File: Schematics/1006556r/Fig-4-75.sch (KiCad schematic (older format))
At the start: 0 parts

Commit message: For module A31, transcribed through Fig 4-87, leaving just 88, 91, 93, 114, 141, and 147 to go, plus their integration into the top-level sheet (and resolution of remaining inconsistencies in ND-1021041).
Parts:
- added J1: ConnectorGeneric, symbol AGC_DSKY:ConnectorGeneric
- added U? (x14): D3NOR-+3VDC-0VDC-nd1021041-A_C-___, symbol D3NOR-+3VDC-0VDC-nd1021041:D3NOR-+3VDC-0VDC-nd1021041-A_C-___
- added U? (x4): D3NOR-+3VDC-0VDC-nd1021041-ABC-___, symbol D3NOR-+3VDC-0VDC-nd1021041:D3NOR-+3VDC-0VDC-nd1021041-ABC-___
- added U? (x4): D3NOR-NC-0VDC-expander-nd1021041-A_C-___, symbol D3NOR-NC-0VDC-expander-nd1021041:D3NOR-NC-0VDC-expander-nd1021041-A_C-___
- added U?: D3NOR-+3VDC-0VDC-nd1021041-_B_-___, symbol D3NOR-+3VDC-0VDC-nd1021041:D3NOR-+3VDC-0VDC-nd1021041-_B_-___
- added U?: D3NOR-NC-0VDC-expander-nd1021041-ABC-___, symbol D3NOR-NC-0VDC-expander-nd1021041:D3NOR-NC-0VDC-expander-nd1021041-ABC-___
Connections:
- net +3VDC: now also U?.6 (+3VDC), U?.6 (+3VDC), U?.6 (+3VDC), U?.6 (+3VDC), U?.6 (+3VDC), U?.6 (+3VDC), U?.6 (+3VDC), U?.6 (+3VDC), U?.6 (+3VDC), U?.6 (+3VDC), U?.6 (+3VDC), U?.6 (+3VDC), U?.6 (+3VDC), U?.6 (+3VDC), U?.6 (+3VDC), U?.6 (+3VDC), U?.6 (+3VDC), U?.6 (+3VDC), U?.6 (+3VDC)
- net 0VDC: now also U?.2 (0VDC), U?.3 (0VDC), U?.3 (0VDC), U?.3 (0VDC), U?.3 (0VDC), U?.3 (0VDC), U?.3 (0VDC), U?.3 (0VDC), U?.3 (0VDC), U?.3 (0VDC), U?.3 (0VDC), U?.3 (0VDC), U?.3 (0VDC), U?.3 (0VDC), U?.3 (0VDC), U?.3 (0VDC), U?.3 (0VDC), U?.3 (0VDC), U?.3 (0VDC), U?.4 (0VDC), U?.5 (0VDC), U?.5 (0VDC), U?.5 (0VDC), U?.5 (0VDC), U?.5 (0VDC), U?.5 (0VDC), U?.5 (0VDC), U?.5 (0VDC), U?.5 (0VDC), U?.5 (0VDC), U?.5 (0VDC), U?.5 (0VDC), U?.5 (0VDC), U?.5 (0VDC), U?.5 (0VDC), U?.5 (0VDC), U?.5 (0VDC), U?.5 (0VDC), U?.5 (0VDC), U?.5 (0VDC), U?.5 (0VDC), U?.5 (0VDC), U?.5 (0VDC), U?.5 (0VDC)
- new net: J1.81, U?.1 (J), U?.2 (C)
- new net: J1.63, U?.2 (C)
- new net: J1.82, U?.4 (A)
- new net: J1.85, U?.2 (C)
- new net: J1.116, U?.4 (A)
- new net: J1.139, U?.4 (A), U?.4 (A)
- new net: J1.89, U?.4 (A)
- new net: J1.137, U?.4 (A)
- new net: J1.61, U?.2 (C)
- new net: J1.135, U?.2 (C)
- new net: J1.41, U?.4 (A), U?.4 (A)
- new net: J1.65, U?.4 (A)
- new net: J1.42, U?.1 (J)
- new net: U?.1 (J), U?.4 (A) (x4)
- new net: U?.1 (J), U?.3 (B) (x2)
- new net: J1.123, U?.2 (C), U?.3 (B)
- new net: J1.53, U?.2 (C), U?.4 (A)
- new net: U?.1 (J), U?.2 (C) (x4)
- new net: J1.136, U?.4 (A), U?.4 (A), U?.4 (A)
- new net: J1.44, U?.2 (C)
- new net: J1.46, U?.4 (A)
- new net: U?.1 (J), U?.2 (C), U?.3 (B)
- new net: J1.83, U?.3 (B)
- new net: U?.1 (J), U?.2 (C), U?.2 (C)
- new net: J1.100, U?.2 (C)
- new net: J1.98, U?.2 (C)
- new net: J1.86, U?.1 (J), U?.1 (J)
- new net: J1.50, U?.2 (C)
- new net: J1.57, U?.1 (J), U?.3 (B)
- new net: J1.69, U?.4 (A)
- new net: J1.109, U?.4 (A)
- new net: J1.103, U?.2 (C)
- new net: J1.101, U?.1 (J)
- new net: J1.104, U?.2 (C)
- new net: J1.105, U?.2 (C)
- new net: J1.67, U?.2 (C)
- new net: J1.73, U?.1 (J), U?.1 (J)
- new net: J1.99, U?.2 (C)
- new net: U?.1 (J), U?.4 (A), U?.4 (A)
- new net: U?.1 (J), U?.1 (J), U?.4 (A)
- new net: J1.77, U?.1 (J)
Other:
- note added: "Notes from the Virtual AGC Project:\n5. Figure 4-75 duplicates the circuits for gates 60007 and\n 60056, but is not internally consistent with respect to\n either the type of gate or the numbering of the connector\n pins feeding the gates. The numbering has been \n reconciled by referencing the other ND-1021041 Figures\n comprising module A21. — RSB 2018"

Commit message: Finished up transcription of drawing 1006556 (Block I logic flow S, module A21).  But it may be a total mess, so user beware!
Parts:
- removed unit 63 of J1
- removed unit 82 of J1
- removed unit 116 of J1
- removed unit 139 of J1
- removed unit 89 of J1
- removed unit 137 of J1
- removed unit 61 of J1
- removed unit 41 of J1
- removed unit 65 of J1
- removed unit 53 of J1
- removed unit 83 of J1
- removed unit 50 of J1
- removed unit 109 of J1
- removed unit 103 of J1
- removed unit 67 of J1
- removed unit 123 of J1
- removed unit 98 of J1
- removed unit 99 of J1
- removed unit 136 of J1
- removed U? (x6): D3NOR-+3VDC-0VDC-nd1021041-A_C-___, symbol D3NOR-+3VDC-0VDC-nd1021041:D3NOR-+3VDC-0VDC-nd1021041-A_C-___
- gave numbers to parts that had none: 18
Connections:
- net T04_B: now reaches U610.4 (A)
- net BR1: now reaches U603.4 (A)
- net T02_: now reaches U609.4 (A)
- net G06: now reaches U602.4 (A)
- net g60052: now reaches J1.42, U605.1 (J)
- net g60031: now reaches U609.1 (J), U612.4 (A)
- net g60014: now reaches U611.3 (B)
- net MP1_: now reaches U616.3 (B)
- net T01_: now reaches U608.2 (C)
- net g60034: now reaches U611.2 (C)
- net T04_: now reaches U605.4 (A), U606.4 (A), U607.4 (A)
- net g60056: now reaches U610.1 (J), U612.2 (C), U615.3 (B)
- net TS0_: now reaches U610.3 (B)
- net g60057: now reaches U606.1 (J), U613.2 (C), U615.2 (C)
- net g60072: now reaches U614.2 (C)
- net T03_: now reaches U616.4 (A)
- net g60062: now reaches U617.2 (C)
- net g60067: now reaches U612.3 (B)
- net STD2: now reaches U601.2 (C)
- net g60048: now reaches U613.4 (A)
- net TC: now reaches U602.2 (C)
- net g60047: now reaches U616.1 (J), U617.4 (A)

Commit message: When I started recovering transcribed Block I schematics from document ND-1021041, there was no info available to me on the pinout of the NOR-gates they used, and it didn't occur to me that any might be forthcoming, so I chose a pinout arbitrarily.  It turns out that we now have the required info (SCD 1006771), and my arbitrary choices were wrong. I've therefore updated the NOR-library generator script, the relevant NOR libraries themselves, and all of the so-far-recovered Block I schematics using those gates.  It doesn't really matter in the cosmic sense, since the real Block I schematics have become available in the meantime, so that these recovered schematics are of less interest, but it will come in handy when I eventually want to do cross-checking.  I haven't checked these updated schematics in full detail, but I've spot-checked them, and run some ERCs and netlists, and it looks good to me.
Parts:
- U601, U613, U614, U617: value D3NOR-NC-0VDC-expander-nd1021041-A_C-___ -> D3NOR-NC-0VDC-expander-nd1021041-1_5-___; symbol D3NOR-NC-0VDC-expander-nd1021041:D3NOR-NC-0VDC-expander-nd1021041-A_C-___ -> D3NOR-NC-0VDC-expander-nd1021041:D3NOR-NC-0VDC-expander-nd1021041-1_5-___
- U602, U603, U604, U605, U606, U607, U608, U609: value D3NOR-+3VDC-0VDC-nd1021041-A_C-___ -> D3NOR-+3VDC-0VDC-nd1021041-1_5-___; symbol D3NOR-+3VDC-0VDC-nd1021041:D3NOR-+3VDC-0VDC-nd1021041-A_C-___ -> D3NOR-+3VDC-0VDC-nd1021041:D3NOR-+3VDC-0VDC-nd1021041-1_5-___
- U610, U611, U615, U616: value D3NOR-+3VDC-0VDC-nd1021041-ABC-___ -> D3NOR-+3VDC-0VDC-nd1021041-135-___; symbol D3NOR-+3VDC-0VDC-nd1021041:D3NOR-+3VDC-0VDC-nd1021041-ABC-___ -> D3NOR-+3VDC-0VDC-nd1021041:D3NOR-+3VDC-0VDC-nd1021041-135-___
- U612: value D3NOR-NC-0VDC-expander-nd1021041-ABC-___ -> D3NOR-NC-0VDC-expander-nd1021041-135-___; symbol D3NOR-NC-0VDC-expander-nd1021041:D3NOR-NC-0VDC-expander-nd1021041-ABC-___ -> D3NOR-NC-0VDC-expander-nd1021041:D3NOR-NC-0VDC-expander-nd1021041-135-___
- U618: value D3NOR-+3VDC-0VDC-nd1021041-_B_-___ -> D3NOR-+3VDC-0VDC-nd1021041-_3_-___; symbol D3NOR-+3VDC-0VDC-nd1021041:D3NOR-+3VDC-0VDC-nd1021041-_B_-___ -> D3NOR-+3VDC-0VDC-nd1021041:D3NOR-+3VDC-0VDC-nd1021041-_3_-___
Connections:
- net +3VDC: now also U602.8 (+3VDC), U603.8 (+3VDC), U604.8 (+3VDC), U605.8 (+3VDC), U606.8 (+3VDC), U607.8 (+3VDC), U608.8 (+3VDC), U609.8 (+3VDC), U610.8 (+3VDC), U611.8 (+3VDC), U615.8 (+3VDC), U616.8 (+3VDC), U618.8 (+3VDC); no longer U602.6 (+3VDC), U603.6 (+3VDC), U604.6 (+3VDC), U605.6 (+3VDC), U606.6 (+3VDC), U607.6 (+3VDC), U608.6 (+3VDC), U609.6 (+3VDC), U610.6 (+3VDC), U611.6 (+3VDC), U615.6 (+3VDC), U616.6 (+3VDC), U618.6 (+3VDC)
- net 0VDC: now also U601.4 (0VDC), U602.4 (0VDC), U603.4 (0VDC), U604.4 (0VDC), U605.4 (0VDC), U606.4 (0VDC), U607.4 (0VDC), U608.4 (0VDC), U609.4 (0VDC), U610.4 (0VDC), U611.4 (0VDC), U612.4 (0VDC), U613.4 (0VDC), U614.4 (0VDC), U615.4 (0VDC), U616.4 (0VDC), U617.4 (0VDC), U618.1 (0VDC); no longer U601.5 (0VDC), U602.5 (0VDC), U603.5 (0VDC), U604.5 (0VDC), U605.5 (0VDC), U606.5 (0VDC), U607.5 (0VDC), U608.5 (0VDC), U609.5 (0VDC), U610.5 (0VDC), U611.5 (0VDC), U612.5 (0VDC), U613.5 (0VDC), U614.5 (0VDC), U615.5 (0VDC), U616.5 (0VDC), U617.5 (0VDC), U618.2 (0VDC)
- net BR1: now also U603.1; no longer U603.4 (A)
- net G06: now also U602.1; no longer U602.4 (A)
- net STD2: now also U601.5; no longer U601.2 (C)
- net T01_: now also U608.5; no longer U608.2 (C)
- net T02_: now also U609.1; no longer U609.4 (A)
- net T03_: now also U616.1; no longer U616.4 (A)
- net T04_: now also U605.1, U606.1, U607.1; no longer U605.4 (A), U606.4 (A), U607.4 (A)
- net T04_B: now also U610.1; no longer U610.4 (A)
- net TC: now also U602.5; no longer U602.2 (C)
- net g60031: now also U609.7, U612.1; no longer U609.1 (J), U612.4 (A)
- net g60034: now also U611.5; no longer U611.2 (C)
- net g60047: now also U616.7, U617.1; no longer U616.1 (J), U617.4 (A)
- net g60048: now also U613.1; no longer U613.4 (A)
- net g60052: now also U605.7; no longer U605.1 (J)
- net g60056: now also U610.7, U612.5; no longer U610.1 (J), U612.2 (C)
- net g60057: now also U606.7, U613.5, U615.5; no longer U606.1 (J), U613.2 (C), U615.2 (C)
- net g60062: now also U617.5; no longer U617.2 (C)
- net g60072: now also U614.5; no longer U614.2 (C)
- net at J1.85: now also U603.5; no longer U603.2 (C)
- net at J1.135: now also U609.5; no longer U609.2 (C)
- net at U605.2 (NC): no longer U604.1 (J)
- net at U604.2 (NC): no longer J1.44
- net at J1.46: now also U604.1; no longer U604.4 (A)
- net at U606.2 (NC): no longer J1.100
- net at J1.57, U618.3: now also U615.7; no longer U615.1 (J)
- net at J1.69: now also U601.1; no longer U601.4 (A)
- net at J1.101: now also U617.7; no longer U617.1 (J)
- net at U607.2 (NC): no longer J1.104
- net at J1.105: now also U616.5; no longer U616.2 (C)
- net at J1.77: now also U618.7; no longer U618.1 (J)
- new net: J1.81, U603.7, U610.5
- new net: U604.7, U605.5
- new net: J1.44, U604.5
- new net: J1.100, U606.5
- new net: J1.86, U613.7, U614.7
- new net: J1.104, U607.5
- new net: U607.7, U614.1
- new net: J1.73, U611.7, U612.7
- new net: U601.7, U602.7, U608.1
- new net: U608.7, U611.1, U615.1
- now unconnected: U610.2 (C)
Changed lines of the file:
@@
 $EndComp
 $Comp
-L D3NOR-+3VDC-0VDC-nd1021041:D3NOR-+3VDC-0VDC-nd1021041-A_C-___ U609
+L D3NOR-+3VDC-0VDC-nd1021041:D3NOR-+3VDC-0VDC-nd1021041-1_5-___ U609
 U 1 1 5BFAE892
 P 7650 5150
 F 0 "U609" H 7650 5475 140 0001 C CNB
-F 1 "D3NOR-+3VDC-0VDC-nd1021041-A_C-___" H 7650 5575 140 0001 C CNN
+F 1 "D3NOR-+3VDC-0VDC-nd1021041-1_5-___" H 7650 5575 140 0001 C CNN
 F 2 "" H 7650 5625 140 0001 C CNN
 F 3 "" H 7650 5625 140 0001 C CNN
@@
 $EndComp
 $Comp
-L D3NOR-+3VDC-0VDC-nd1021041:D3NOR-+3VDC-0VDC-nd1021041-A_C-___ U605
+L D3NOR-+3VDC-0VDC-nd1021041:D3NOR-+3VDC-0VDC-nd1021041-1_5-___ U605
 U 1 1 5BFAE895
 P 7100 15125
 F 0 "U605" H 7100 15450 140 0001 C CNB
-F 1 "D3NOR-+3VDC-0VDC-nd1021041-A_C-___" H 7100 15550 140 0001 C CNN
+F 1 "D3NOR-+3VDC-0VDC-nd1021041-1_5-___" H 7100 15550 140 0001 C CNN
 F 2 "" H 7100 15600 140 0001 C CNN
 F 3 "" H 7100 15600 140 0001 C CNN
@@
 $EndComp
 $Comp
-L D3NOR-+3VDC-0VDC-nd1021041:D3NOR-+3VDC-0VDC-nd1021041-A_C-___ U604
+L D3NOR-+3VDC-0VDC-nd1021041:D3NOR-+3VDC-0VDC-nd1021041-1_5-___ U604
 U 1 1 5BFAE896
 P 5150 15475
 F 0 "U604" H 5150 15800 140 0001 C CNB
-F 1 "D3NOR-+3VDC-0VDC-nd1021041-A_C-___" H 5150 15900 140 0001 C CNN
+F 1 "D3NOR-+3VDC-0VDC-nd1021041-1_5-___" H 5150 15900 140 0001 C CNN
 F 2 "" H 5150 15950 140 0001 C CNN
 F 3 "" H 5150 15950 140 0001 C CNN
@@
 $EndComp
 $Comp
-L D3NOR-+3VDC-0VDC-nd1021041:D3NOR-+3VDC-0VDC-nd1021041-ABC-___ U610
+L D3NOR-+3VDC-0VDC-nd1021041:D3NOR-+3VDC-0VDC-nd1021041-135-___ U610
 U 1 1 5BFAE897
 P 7650 7525
 F 0 "U610" H 7650 7850 140 0001 C CNB
-F 1 "D3NOR-+3VDC-0VDC-nd1021041-ABC-___" H 7650 7950 140 0001 C CNN
+F 1 "D3NOR-+3VDC-0VDC-nd1021041-135-___" H 7650 7950 140 0001 C CNN
 F 2 "" H 7650 8000 140 0001 C CNN
 F 3 "" H 7650 8000 140 0001 C CNN
@@
 $EndComp
 $Comp
-L D3NOR-+3VDC-0VDC-nd1021041:D3NOR-+3VDC-0VDC-nd1021041-A_C-___ U606
+L D3NOR-+3VDC-0VDC-nd1021041:D3NOR-+3VDC-0VDC-nd1021041-1_5-___ U606
 U 1 1 5BFAE898
 P 7600 9925
 F 0 "U606" H 7600 10250 140 0001 C CNB
-F 1 "D3NOR-+3VDC-0VDC-nd1021041-A_C-___" H 7600 10350 140 0001 C CNN
+F 1 "D3NOR-+3VDC-0VDC-nd1021041-1_5-___" H 7600 10350 140 0001 C CNN
 F 2 "" H 7600 10400 140 0001 C CNN
 F 3 "" H 7600 10400 140 0001 C CNN
@@
 $EndComp
 $Comp
-L D3NOR-+3VDC-0VDC-nd1021041:D3NOR-+3VDC-0VDC-nd1021041-A_C-___ U603
+L D3NOR-+3VDC-0VDC-nd1021041:D3NOR-+3VDC-0VDC-nd1021041-1_5-___ U603
 U 1 1 5BFAE899
 P 3025 7875
 F 0 "U603" H 3025 8200 140 0001 C CNB
-F 1 "D3NOR-+3VDC-0VDC-nd1021041-A_C-___" H 3025 8300 140 0001 C CNN
+F 1 "D3NOR-+3VDC-0VDC-nd1021041-1_5-___" H 3025 8300 140 0001 C CNN
 F 2 "" H 3025 8350 140 0001 C CNN
 F 3 "" H 3025 8350 140 0001 C CNN
@@
 $EndComp
 $Comp
-L D3NOR-+3VDC-0VDC-nd1021041:D3NOR-+3VDC-0VDC-nd1021041-A_C-___ U607
+L D3NOR-+3VDC-0VDC-nd1021041:D3NOR-+3VDC-0VDC-nd1021041-1_5-___ U607
 U 1 1 5BFAE8A8
 P 7600 11100
 F 0 "U607" H 7600 11425 140 0001 C CNB
-F 1 "D3NOR-+3VDC-0VDC-nd1021041-A_C-___" H 7600 11525 140 0001 C CNN
+F 1 "D3NOR-+3VDC-0VDC-nd1021041-1_5-___" H 7600 11525 140 0001 C CNN
 F 2 "" H 7600 11575 140 0001 C CNN
 F 3 "" H 7600 11575 140 0001 C CNN
@@
 $EndComp
 $Comp
-L D3NOR-NC-0VDC-expander-nd1021041:D3NOR-NC-0VDC-expander-nd1021041-A_C-___ U614
+L D3NOR-NC-0VDC-expander-nd1021041:D3NOR-NC-0VDC-expander-nd1021041-1_5-___ U614
 U 1 1 5BFAE8AE
 P 12850 9575
 F 0 "U614" H 12850 9900 140 0001 C CNB
-F 1 "D3NOR-NC-0VDC-expander-nd1021041-A_C-___" H 12850 10000 140 0001 C CNN
+F 1 "D3NOR-NC-0VDC-expander-nd1021041-1_5-___" H 12850 10000 140 0001 C CNN
 F 2 "" H 12850 10050 140 0001 C CNN
 F 3 "" H 12850 10050 140 0001 C CNN
@@
 $EndComp
 $Comp
-L D3NOR-NC-0VDC-expander-nd1021041:D3NOR-NC-0VDC-expander-nd1021041-A_C-___ U613
+L D3NOR-NC-0VDC-expander-nd1021041:D3NOR-NC-0VDC-expander-nd1021041-1_5-___ U613
 U 1 1 5BFAE8AF
 P 12850 8550
 F 0 "U613" H 12850 8875 140 0001 C CNB
-F 1 "D3NOR-NC-0VDC-expander-nd1021041-A_C-___" H 12850 8975 140 0001 C CNN
+F 1 "D3NOR-NC-0VDC-expander-nd1021041-1_5-___" H 12850 8975 140 0001 C CNN
 F 2 "" H 12850 9025 140 0001 C CNN
 F 3 "" H 12850 9025 140 0001 C CNN
@@
 $EndComp
 $Comp
-L D3NOR-+3VDC-0VDC-nd1021041:D3NOR-+3VDC-0VDC-nd1021041-A_C-___ U608
+L D3NOR-+3VDC-0VDC-nd1021041:D3NOR-+3VDC-0VDC-nd1021041-1_5-___ U608
 U 1 1 5BFAE8B2
 P 7650 1650
 F 0 "U608" H 7650 1975 140 0001 C CNB
-F 1 "D3NOR-+3VDC-0VDC-nd1021041-A_C-___" H 7650 2075 140 0001 C CNN
+F 1 "D3NOR-+3VDC-0VDC-nd1021041-1_5-___" H 7650 2075 140 0001 C CNN
 F 2 "" H 7650 2125 140 0001 C CNN
 F 3 "" H 7650 2125 140 0001 C CNN
@@
 $EndComp
 $Comp
-L D3NOR-NC-0VDC-expander-nd1021041:D3NOR-NC-0VDC-expander-nd1021041-A_C-___ U601
+L D3NOR-NC-0VDC-expander-nd1021041:D3NOR-NC-0VDC-expander-nd1021041-1_5-___ U601
 U 1 1 5BFAE8B4
 P 3000 2400
 F 0 "U601" H 3000 2725 140 0001 C CNB
-F 1 "D3NOR-NC-0VDC-expander-nd1021041-A_C-___" H 3000 2825 140 0001 C CNN
+F 1 "D3NOR-NC-0VDC-expander-nd1021041-1_5-___" H 3000 2825 140 0001 C CNN
 F 2 "" H 3000 2875 140 0001 C CNN
 F 3 "" H 3000 2875 140 0001 C CNN
@@
 $EndComp
 $Comp
-L D3NOR-+3VDC-0VDC-nd1021041:D3NOR-+3VDC-0VDC-nd1021041-A_C-___ U602
+L D3NOR-+3VDC-0VDC-nd1021041:D3NOR-+3VDC-0VDC-nd1021041-1_5-___ U602
 U 1 1 5BFAE8B5
 P 3025 1300
 F 0 "U602" H 3025 1625 140 0001 C CNB
-F 1 "D3NOR-+3VDC-0VDC-nd1021041-A_C-___" H 3025 1725 140 0001 C CNN
+F 1 "D3NOR-+3VDC-0VDC-nd1021041-1_5-___" H 3025 1725 140 0001 C CNN
 F 2 "" H 3025 1775 140 0001 C CNN
 F 3 "" H 3025 1775 140 0001 C CNN
@@
 $EndComp
 $Comp
-L D3NOR-+3VDC-0VDC-nd1021041:D3NOR-+3VDC-0VDC-nd1021041-ABC-___ U616
+L D3NOR-+3VDC-0VDC-nd1021041:D3NOR-+3VDC-0VDC-nd1021041-135-___ U616
 U 1 1 5BFAE8B8
 P 17350 3350
 F 0 "U616" H 17350 3675 140 0001 C CNB
-F 1 "D3NOR-+3VDC-0VDC-nd1021041-ABC-___" H 17350 3775 140 0001 C CNN
+F 1 "D3NOR-+3VDC-0VDC-nd1021041-135-___" H 17350 3775 140 0001 C CNN
 F 2 "" H 17350 3825 140 0001 C CNN
 F 3 "" H 17350 3825 140 0001 C CNN
@@
 $EndComp
 $Comp
-L D3NOR-+3VDC-0VDC-nd1021041:D3NOR-+3VDC-0VDC-nd1021041-_B_-___ U618
+L D3NOR-+3VDC-0VDC-nd1021041:D3NOR-+3VDC-0VDC-nd1021041-_3_-___ U618
 U 1 1 5BFAE8BA
 P 19450 9675
 F 0 "U618" H 19450 10000 140 0001 C CNB
-F 1 "D3NOR-+3VDC-0VDC-nd1021041-_B_-___" H 19450 10100 140 0001 C CNN
+F 1 "D3NOR-+3VDC-0VDC-nd1021041-_3_-___" H 19450 10100 140 0001 C CNN
 F 2 "" H 19450 10150 140 0001 C CNN
 F 3 "" H 19450 10150 140 0001 C CNN
@@
 $EndComp
 $Comp
-L D3NOR-NC-0VDC-expander-nd1021041:D3NOR-NC-0VDC-expander-nd1021041-A_C-___ U617
+L D3NOR-NC-0VDC-expander-nd1021041:D3NOR-NC-0VDC-expander-nd1021041-1_5-___ U617
 U 1 1 5BFAE8BB
 P 19250 3950
 F 0 "U617" H 19250 4275 140 0001 C CNB
-F 1 "D3NOR-NC-0VDC-expander-nd1021041-A_C-___" H 19250 4375 140 0001 C CNN
+F 1 "D3NOR-NC-0VDC-expander-nd1021041-1_5-___" H 19250 4375 140 0001 C CNN
 F 2 "" H 19250 4425 140 0001 C CNN
 F 3 "" H 19250 4425 140 0001 C CNN
@@
 $EndComp
 $Comp
-L D3NOR-+3VDC-0VDC-nd1021041:D3NOR-+3VDC-0VDC-nd1021041-ABC-___ U611
+L D3NOR-+3VDC-0VDC-nd1021041:D3NOR-+3VDC-0VDC-nd1021041-135-___ U611
 U 1 1 5BFAE8BC
 P 12825 6500
 F 0 "U611" H 12825 6825 140 0001 C CNB
-F 1 "D3NOR-+3VDC-0VDC-nd1021041-ABC-___" H 12825 6925 140 0001 C CNN
+F 1 "D3NOR-+3VDC-0VDC-nd1021041-135-___" H 12825 6925 140 0001 C CNN
 F 2 "" H 12825 6975 140 0001 C CNN
 F 3 "" H 12825 6975 140 0001 C CNN
@@
 $EndComp
 $Comp
-L D3NOR-NC-0VDC-expander-nd1021041:D3NOR-NC-0VDC-expander-nd1021041-ABC-___ U612
+L D3NOR-NC-0VDC-expander-nd1021041:D3NOR-NC-0VDC-expander-nd1021041-135-___ U612
 U 1 1 5BFAE8BD
 P 12850 7475
 F 0 "U612" H 12850 7800 140 0001 C CNB
-F 1 "D3NOR-NC-0VDC-expander-nd1021041-ABC-___" H 12850 7900 140 0001 C CNN
+F 1 "D3NOR-NC-0VDC-expander-nd1021041-135-___" H 12850 7900 140 0001 C CNN
 F 2 "" H 12850 7950 140 0001 C CNN
 F 3 "" H 12850 7950 140 0001 C CNN
@@
 $EndComp
 $Comp
-L D3NOR-+3VDC-0VDC-nd1021041:D3NOR-+3VDC-0VDC-nd1021041-ABC-___ U615
+L D3NOR-+3VDC-0VDC-nd1021041:D3NOR-+3VDC-0VDC-nd1021041-135-___ U615
 U 1 1 5BFAE8BE
 P 17325 10900
 F 0 "U615" H 17325 11225 140 0001 C CNB
-F 1 "D3NOR-+3VDC-0VDC-nd1021041-ABC-___" H 17325 11325 140 0001 C CNN
+F 1 "D3NOR-+3VDC-0VDC-nd1021041-135-___" H 17325 11325 140 0001 C CNN
 F 2 "" H 17325 11375 140 0001 C CNN
 F 3 "" H 17325 11375 140 0001 C CNN

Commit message: Made various fixes in cross-checking 1006556A vs 1006556r, but netlistCompare.py isn't fully working for some reason, so more work needs to be done on it.
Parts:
- U618: Location 60515 -> 60415
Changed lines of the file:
@@
 L AGC_DSKY:ConnectorGeneric J1
 U 77 1 5BFAE8B6
-P 20800 9650
-F 0 "J1" H 20800 9975 140 0001 C CNN
-F 1 "ConnectorGeneric" H 20800 10075 140 0001 C CNN
-F 2 "" H 20800 10125 140 0001 C CNN
-F 3 "" H 20800 10125 140 0001 C CNN
-F 4 "CI" H 20350 9575 140 0000 C BNB "Caption"
-	77   20800 9650
+P 20800 9675
+F 0 "J1" H 20800 10000 140 0001 C CNN
+F 1 "ConnectorGeneric" H 20800 10100 140 0001 C CNN
+F 2 "" H 20800 10150 140 0001 C CNN
+F 3 "" H 20800 10150 140 0001 C CNN
+F 4 "CI" H 20350 9600 140 0000 C BNB "Caption"
+	77   20800 9675
 	-1   0    0    1
 $EndComp
@@
 F 2 "" H 19450 10150 140 0001 C CNN
 F 3 "" H 19450 10150 140 0001 C CNN
-F 4 "60515" H 19450 9675 140 0000 C CNB "Location"
+F 4 "60415" H 19450 9675 140 0000 C CNB "Location"
 	1    19450 9675
 	1    0    0    1
@@
 	18525 10900 19050 10900
 Wire Wire Line
-	20350 9675 20525 9650
+	20350 9675 20525 9675
 Wire Wire Line
 	6050 15475 6475 15475

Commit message: Schematics 1006556r and 1006556A have been cross-checked and corrected, insofar as it is possible to do so, given that 1006556r (from ND-1021041) appears to be a later revision with some electrical changes.
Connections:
- net g60057: no longer U615.5
- net g60067: now also U615.5
- net BR1 renamed BR1A
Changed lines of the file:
@@
 	9500 9925 9500 8900
 Wire Wire Line
-	9500 8900 11750 8900
-Wire Wire Line
 	8525 8700 8925 8700
 Wire Wire Line
@@
 	9500 6400 9500 7475
 Wire Wire Line
-	9500 7475 12250 7475
+	9500 7475 11200 7475
 Wire Wire Line
 	8550 5150 8900 5150
@@
 Wire Wire Line
 	11650 5925 11650 6150
-Wire Wire Line
-	11750 8900 11750 11250
-Wire Wire Line
-	11750 11250 16700 11250
-Connection ~ 11750 8900
-Wire Wire Line
-	11750 8900 12225 8900
 Wire Wire Line
 	3925 7875 4100 7875
@@
 TC
 Text HLabel 1975 7525 0    140  Input ~ 28
-BR1
+BR1A
 Text HLabel 6600 7525 0    140  Input ~ 28
 TS0_
+Wire Wire Line
+	9500 8900 12225 8900
+Wire Wire Line
+	11200 7475 11200 11250
+Wire Wire Line
+	11200 11250 16700 11250
+Connection ~ 11200 7475
+Wire Wire Line
+	11200 7475 12250 7475
 $EndSCHEMATC

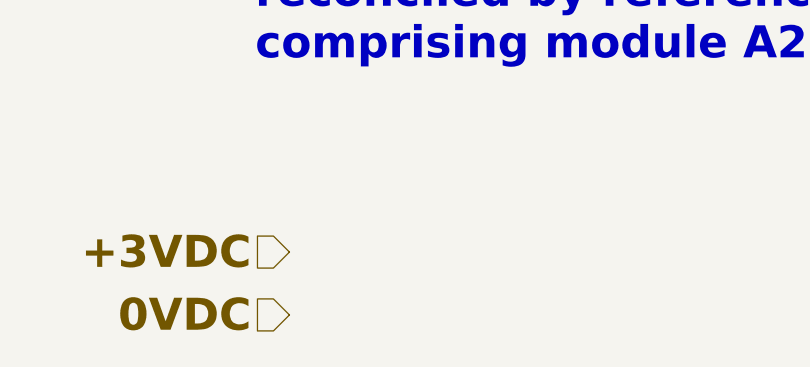
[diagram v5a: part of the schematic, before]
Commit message: Visual fixes were made using eelint, and some nominal electrical changes were made to accommodate current state of KiCad ERC capability. Nevertheless, ERC does not pass, due (I think) to current bugs in KiCad ERC.  Netlist changes are purely nominal, and relate to the addition of non-functional nodes in the power and ground nets.
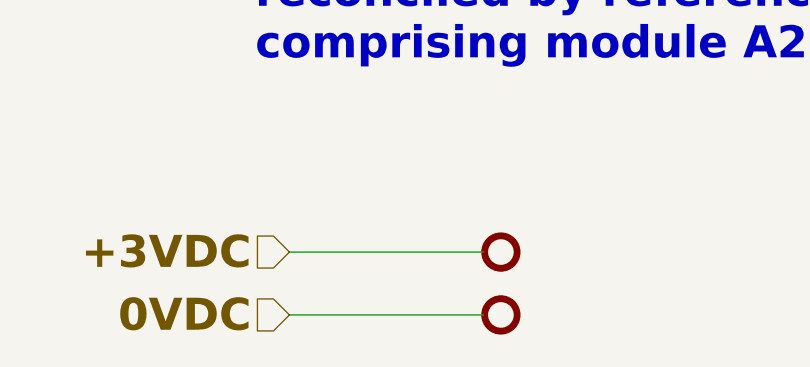
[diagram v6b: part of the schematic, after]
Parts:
- added N601, N602: Node2, symbol AGC_DSKY:Node2
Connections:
- net +3VDC: now also N601.1
- net 0VDC: now also N602.1
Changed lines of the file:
@@
-EESchema Schematic File Version 4
+EESchema Schematic File Version 5
 LIBS:module-cache
 EELAYER 29 0
@@
 Wire Wire Line
 	11200 7475 12250 7475
+$Comp
+L AGC_DSKY:Node2 N?
+U 1 1 5CE28183
+P 15950 15950
+AR Path="/5F3224B7/5CE28183" Ref="N?"  Part="1"
+AR Path="/5F3216C6/5CE28183" Ref="N601"  Part="1"
+F 0 "N601" H 15950 16050 50  0001 C CNN
+F 1 "Node2" H 15950 16125 50  0001 C CNN
+F 2 "" H 15950 15950 50  0001 C CNN
+F 3 "" H 15950 15950 50  0001 C CNN
+F 4 "+3VDC" H 15875 15950 140 0001 R CNB "Caption"
+	1    15950 15950
+	-1   0    0    1
+$EndComp
+$Comp
+L AGC_DSKY:Node2 N?
+U 1 1 5CE2818C
+P 15950 16225
+AR Path="/5F3224B7/5CE2818C" Ref="N?"  Part="0"
+AR Path="/5F3216C6/5CE2818C" Ref="N602"  Part="1"
+F 0 "N602" H 15950 16325 50  0001 C CNN
+F 1 "Node2" H 15950 16400 50  0001 C CNN
+F 2 "" H 15950 16225 50  0001 C CNN
+F 3 "" H 15950 16225 50  0001 C CNN
+F 4 "0VDC" H 15875 16225 140 0001 R CNB "Caption"
+	1    15950 16225
+	-1   0    0    1
+$EndComp
+Wire Wire Line
+	15025 16225 15875 16225
+Wire Wire Line
+	15025 15950 15875 15950
 $EndSCHEMATC
